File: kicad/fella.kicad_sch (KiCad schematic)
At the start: 0 parts

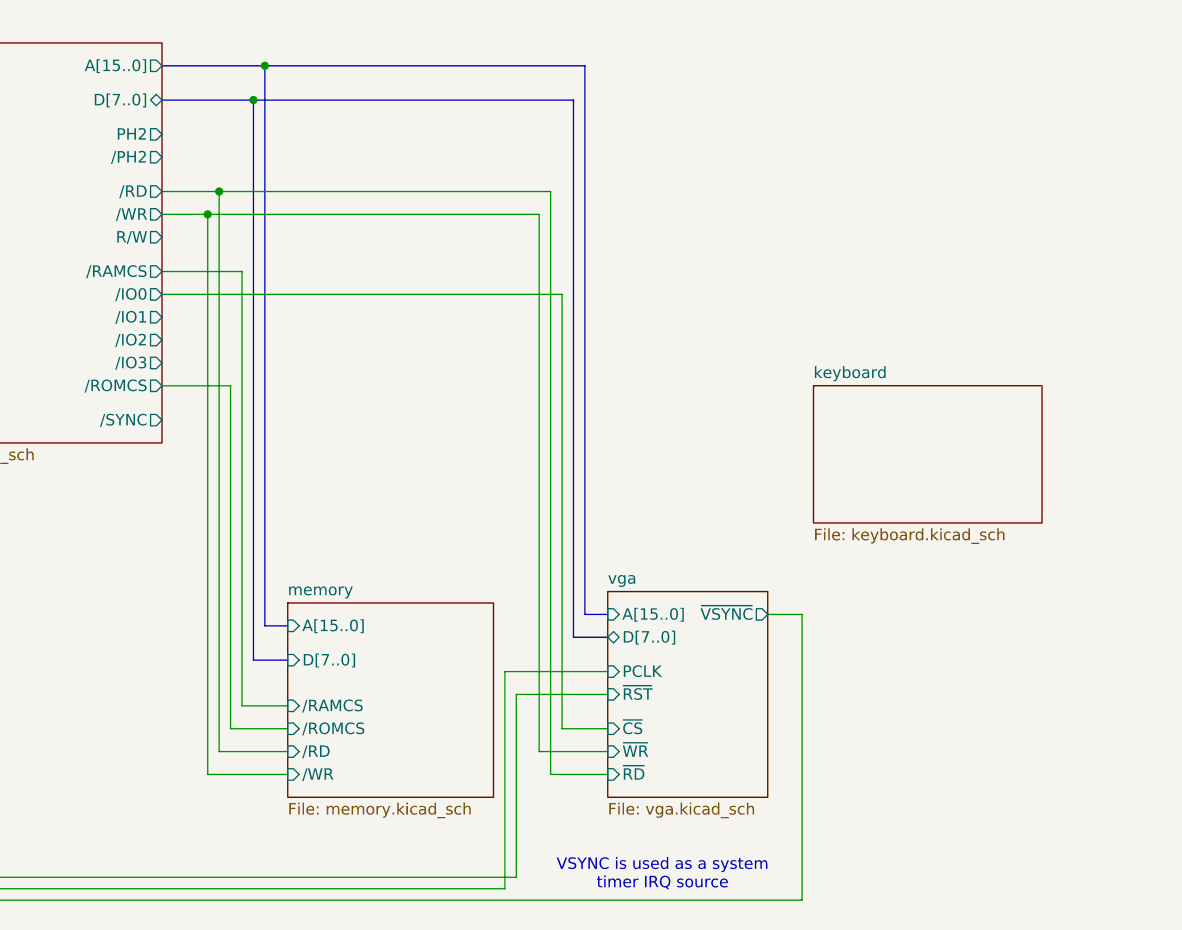
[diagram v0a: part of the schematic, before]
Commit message: Add keyboard connector
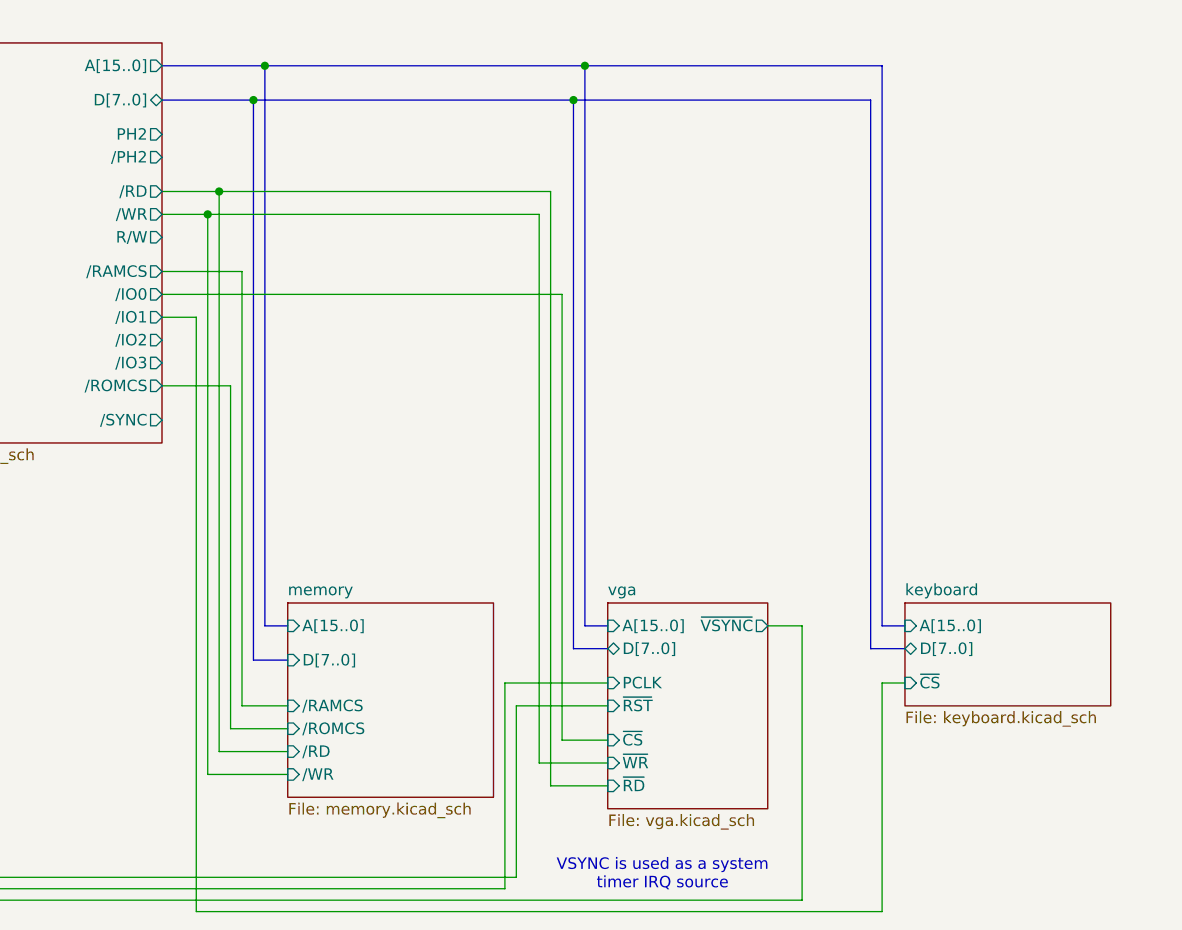
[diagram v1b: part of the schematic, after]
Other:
- sheet keyboard ports: added A[15..0], D[7..0], ~{CS}; removed none
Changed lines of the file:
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@@
+	)
+	(junction
+		(at 161.29 50.8)
+		(diameter 0)
+		(color 0 0 0 0)
 	)
 	(junction
@@
 		(color 0 0 0 0)
 	)
+	(junction
+		(at 160.02 54.61)
+		(diameter 0)
+		(color 0 0 0 0)
+	)
 	(wire
 		(pts
@@
 	(wire
 		(pts
-			(xy 181.61 111.76) (xy 185.42 111.76)
+			(xy 181.61 113.03) (xy 185.42 113.03)
 		)
 		(stroke
@@
 	(bus
 		(pts
-			(xy 161.29 111.76) (xy 161.29 50.8)
+			(xy 161.29 113.03) (xy 161.29 50.8)
 		)
 		(stroke
@@
 		)
 	)
+	(wire
+		(pts
+			(xy 114.3 78.74) (xy 118.11 78.74)
+		)
+		(stroke
+			(width 0)
+			(type default)
+		)
+	)
 	(bus
 		(pts
@@
 	(wire
 		(pts
-			(xy 156.21 67.31) (xy 156.21 127)
-		)
-		(stroke
-			(width 0)
-			(type default)
-		)
-	)
-	(bus
-		(pts
-			(xy 160.02 54.61) (xy 160.02 114.3)
+			(xy 156.21 67.31) (xy 156.21 128.27)
+		)
+		(stroke
+			(width 0)
+			(type default)
+		)
+	)
+	(bus
+		(pts
+			(xy 160.02 54.61) (xy 160.02 115.57)
 		)
 		(stroke
@@
 		)
 	)
+	(bus
+		(pts
+			(xy 194.31 50.8) (xy 161.29 50.8)
+		)
+		(stroke
+			(width 0)
+			(type default)
+		)
+	)
+	(bus
+		(pts
+			(xy 160.02 54.61) (xy 193.04 54.61)
+		)
+		(stroke
+			(width 0)
+			(type default)
+		)
+	)
 	(wire
 		(pts
@@
 	(bus
 		(pts
-			(xy 160.02 114.3) (xy 163.83 114.3)
-		)
-		(stroke
-			(width 0)
-			(type default)
-		)
-	)
-	(wire
-		(pts
-			(xy 158.75 124.46) (xy 163.83 124.46)
+			(xy 193.04 115.57) (xy 196.85 115.57)
+		)
+		(stroke
+			(width 0)
+			(type default)
+		)
+	)
+	(bus
+		(pts
+			(xy 160.02 115.57) (xy 163.83 115.57)
+		)
+		(stroke
+			(width 0)
+			(type default)
+		)
+	)
+	(wire
+		(pts
+			(xy 158.75 125.73) (xy 163.83 125.73)
+		)
+		(stroke
+			(width 0)
+			(type default)
+		)
+	)
+	(bus
+		(pts
+			(xy 193.04 54.61) (xy 193.04 115.57)
+		)
+		(stroke
+			(width 0)
+			(type default)
+		)
+	)
+	(wire
+		(pts
+			(xy 194.31 144.78) (xy 194.31 119.38)
 		)
 		(stroke
@@
 	(wire
 		(pts
-			(xy 157.48 129.54) (xy 163.83 129.54)
+			(xy 157.48 130.81) (xy 163.83 130.81)
+		)
+		(stroke
+			(width 0)
+			(type default)
+		)
+	)
+	(wire
+		(pts
+			(xy 118.11 78.74) (xy 118.11 144.78)
 		)
 		(stroke
@@
 	(wire
 		(pts
+			(xy 194.31 119.38) (xy 196.85 119.38)
+		)
+		(stroke
+			(width 0)
+			(type default)
+		)
+	)
+	(wire
+		(pts
 			(xy 119.38 67.31) (xy 119.38 129.54)
 		)
@@
 		)
 	)
+	(bus
+		(pts
+			(xy 196.85 113.03) (xy 194.31 113.03)
+		)
+		(stroke
+			(width 0)
+			(type default)
+		)
+	)
 	(wire
 		(pts
@@
 	(wire
 		(pts
-			(xy 158.75 76.2) (xy 158.75 124.46)
+			(xy 118.11 144.78) (xy 194.31 144.78)
+		)
+		(stroke
+			(width 0)
+			(type default)
+		)
+	)
+	(wire
+		(pts
+			(xy 158.75 76.2) (xy 158.75 125.73)
 		)
 		(stroke
@@
 	(wire
 		(pts
-			(xy 153.67 140.97) (xy 153.67 120.65)
+			(xy 153.67 140.97) (xy 153.67 121.92)
 		)
 		(stroke
@@
 	(wire
 		(pts
-			(xy 156.21 127) (xy 163.83 127)
-		)
-		(stroke
-			(width 0)
-			(type default)
-		)
-	)
-	(wire
-		(pts
-			(xy 153.67 120.65) (xy 163.83 120.65)
-		)
-		(stroke
-			(width 0)
-			(type default)
-		)
-	)
-	(wire
-		(pts
-			(xy 152.4 118.11) (xy 163.83 118.11)
-		)
-		(stroke
-			(width 0)
-			(type default)
-		)
-	)
-	(bus
-		(pts
-			(xy 163.83 111.76) (xy 161.29 111.76)
-		)
-		(stroke
-			(width 0)
-			(type default)
-		)
-	)
-	(wire
-		(pts
-			(xy 185.42 111.76) (xy 185.42 143.51)
+			(xy 156.21 128.27) (xy 163.83 128.27)
+		)
+		(stroke
+			(width 0)
+			(type default)
+		)
+	)
+	(wire
+		(pts
+			(xy 153.67 121.92) (xy 163.83 121.92)
+		)
+		(stroke
+			(width 0)
+			(type default)
+		)
+	)
+	(wire
+		(pts
+			(xy 152.4 119.38) (xy 163.83 119.38)
+		)
+		(stroke
+			(width 0)
+			(type default)
+		)
+	)
+	(bus
+		(pts
+			(xy 163.83 113.03) (xy 161.29 113.03)
+		)
+		(stroke
+			(width 0)
+			(type default)
+		)
+	)
+	(wire
+		(pts
+			(xy 185.42 113.03) (xy 185.42 143.51)
 		)
 		(stroke
@@
 	(bus
 		(pts
+			(xy 194.31 113.03) (xy 194.31 50.8)
+		)
+		(stroke
+			(width 0)
+			(type default)
+		)
+	)
+	(bus
+		(pts
 			(xy 114.3 50.8) (xy 125.73 50.8)
 		)
@@
 	(wire
 		(pts
-			(xy 152.4 142.24) (xy 152.4 118.11)
-		)
-		(stroke
-			(width 0)
-			(type default)
-		)
-	)
-	(wire
-		(pts
-			(xy 157.48 64.77) (xy 157.48 129.54)
+			(xy 152.4 142.24) (xy 152.4 119.38)
+		)
+		(stroke
+			(width 0)
+			(type default)
+		)
+	)
+	(wire
+		(pts
+			(xy 157.48 64.77) (xy 157.48 130.81)
 		)
 		(stroke
@@
 	)
 	(sheet
-		(at 186.69 86.36)
-		(size 25.4 15.24)
+		(at 196.85 110.49)
+		(size 22.86 11.43)
 		(fields_autoplaced yes)
 		(stroke
@@
 		)
 		(property "Sheetname" "keyboard"
-			(at 186.69 85.6484 0)
+			(at 196.85 109.7784 0)
 			(effects
 				(font
@@
 		)
 		(property "Sheetfile" "keyboard.kicad_sch"
-			(at 186.69 102.1846 0)
+			(at 196.85 122.5046 0)
 			(effects
 				(font
@@
 				)
 				(justify left top)
+			)
+		)
+		(pin "A[15..0]" input
+			(at 196.85 113.03 180)
+			(effects
+				(font
+					(size 1.27 1.27)
+				)
+				(justify left)
+			)
+		)
+		(pin "~{CS}" input
+			(at 196.85 119.38 180)
+			(effects
+				(font
+					(size 1.27 1.27)
+				)
+				(justify left)
+			)
+		)
+		(pin "D[7..0]" tri_state
+			(at 196.85 115.57 180)
+			(effects
+				(font
+					(size 1.27 1.27)
+				)
+				(justify left)
 			)
 		)
@@
 	)
 	(sheet
-		(at 163.83 109.22)
+		(at 163.83 110.49)
 		(size 17.78 22.86)
 		(fields_autoplaced yes)
@@
 		)
 		(property "Sheetname" "vga"
-			(at 163.83 108.5084 0)
+			(at 163.83 109.7784 0)
 			(effects
 				(font
@@
 		)
 		(property "Sheetfile" "vga.kicad_sch"
-			(at 163.83 132.6646 0)
+			(at 163.83 133.9346 0)
 			(effects
 				(font
@@
 		)
 		(pin "~{RST}" input
-			(at 163.83 120.65 180)
+			(at 163.83 121.92 180)
 			(effects
 				(font
@@
 		)
 		(pin "PCLK" input
-			(at 163.83 118.11 180)
+			(at 163.83 119.38 180)
 			(effects
 				(font
@@
 		)
 		(pin "~{WR}" input
-			(at 163.83 127 180)
+			(at 163.83 128.27 180)
 			(effects
 				(font
@@
 		)
 		(pin "A[15..0]" input
-			(at 163.83 111.76 180)
+			(at 163.83 113.03 180)
 			(effects
 				(font
@@
 		)
 		(pin "D[7..0]" bidirectional
-			(at 163.83 114.3 180)
+			(at 163.83 115.57 180)
 			(effects
 				(font
@@
 		)
 		(pin "~{RD}" input
-			(at 163.83 129.54 180)
+			(at 163.83 130.81 180)
 			(effects
 				(font
@@
 		)
 		(pin "~{CS}" input
-			(at 163.83 124.46 180)
+			(at 163.83 125.73 180)
 			(effects
 				(font
@@
 		)
 		(pin "~{VSYNC}" output
-			(at 181.61 111.76 0)
-			(effects
-				(font
+			(at 181.61 113.03 0)
+			(effects
+				(font

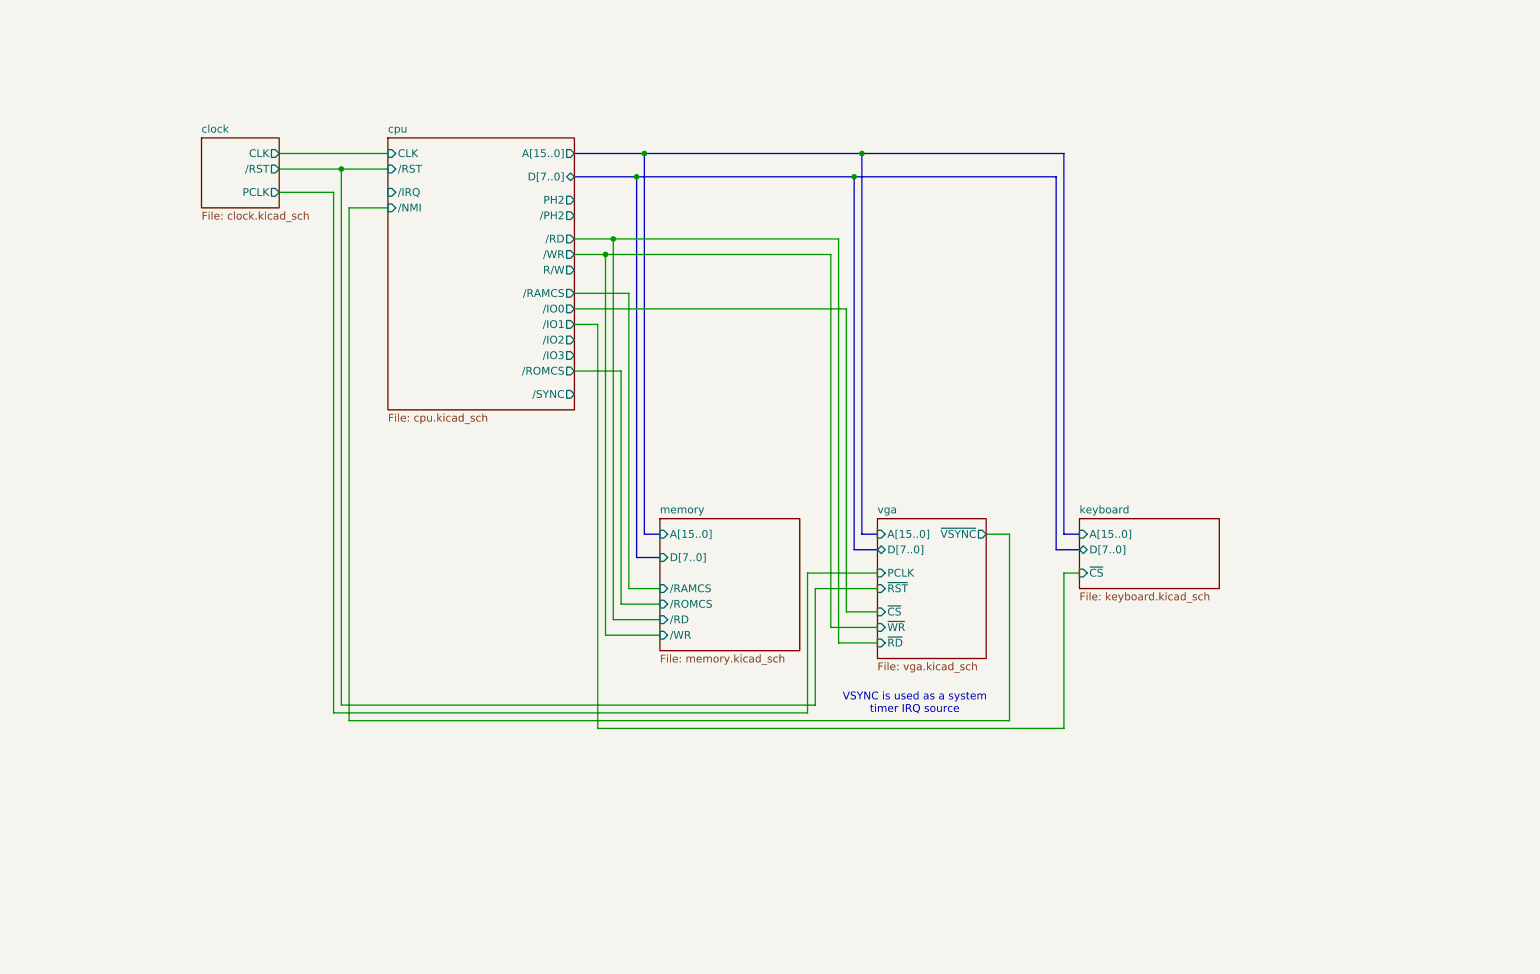
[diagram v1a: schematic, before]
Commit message: Add user IO and USB
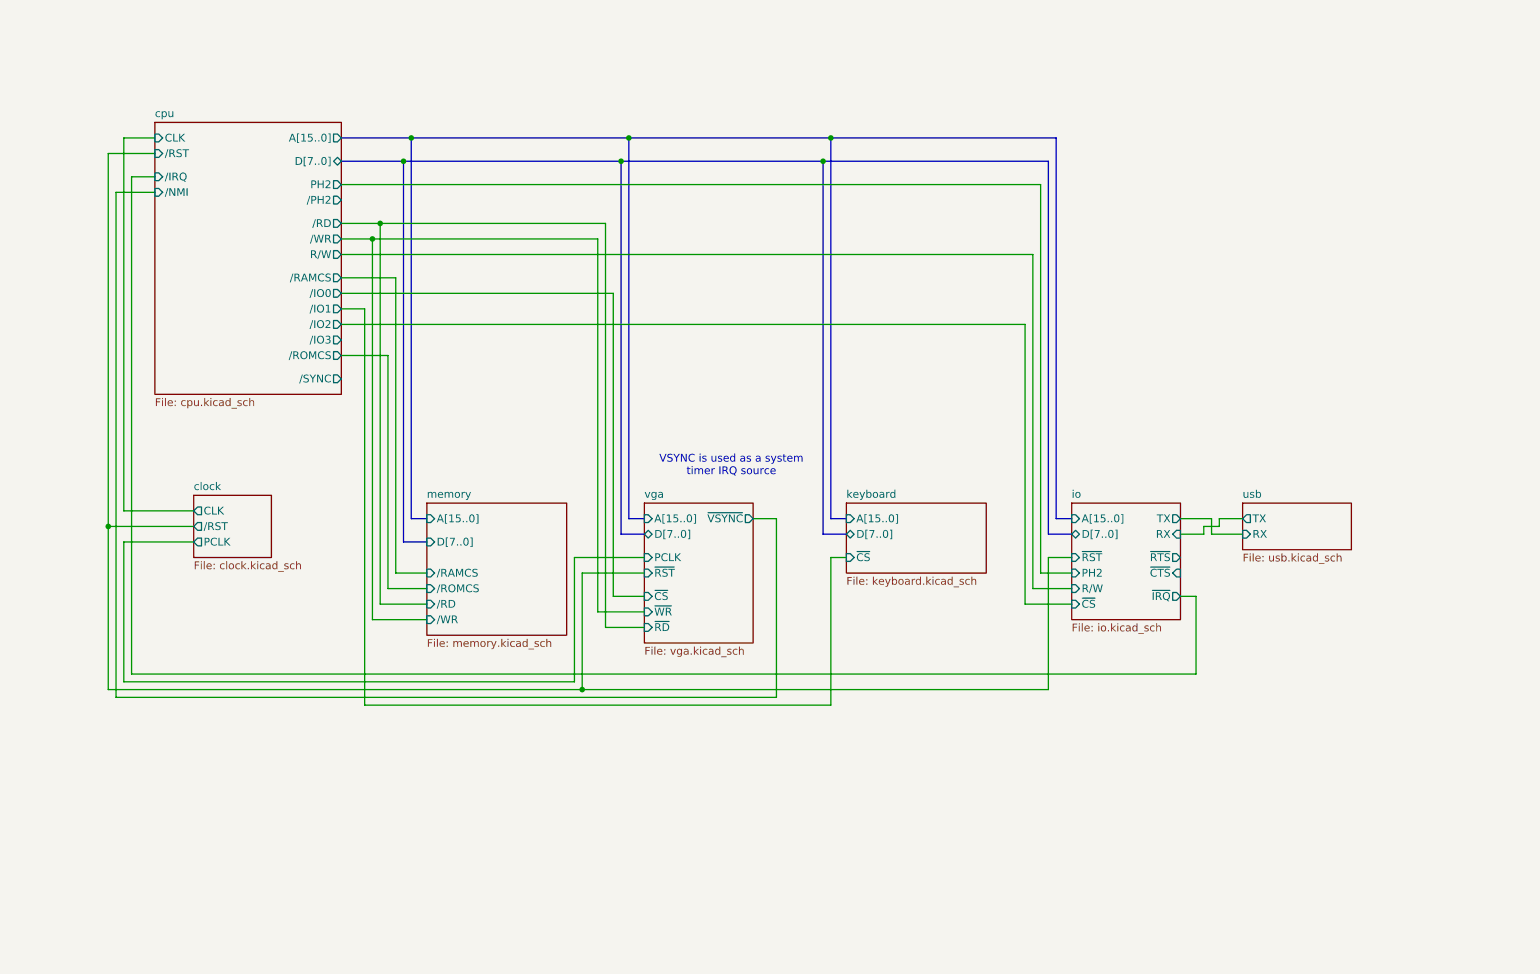
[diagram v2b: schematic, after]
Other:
- added sheet io (io.kicad_sch)
- added sheet usb (usb.kicad_sch)

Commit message: Add expansion slot
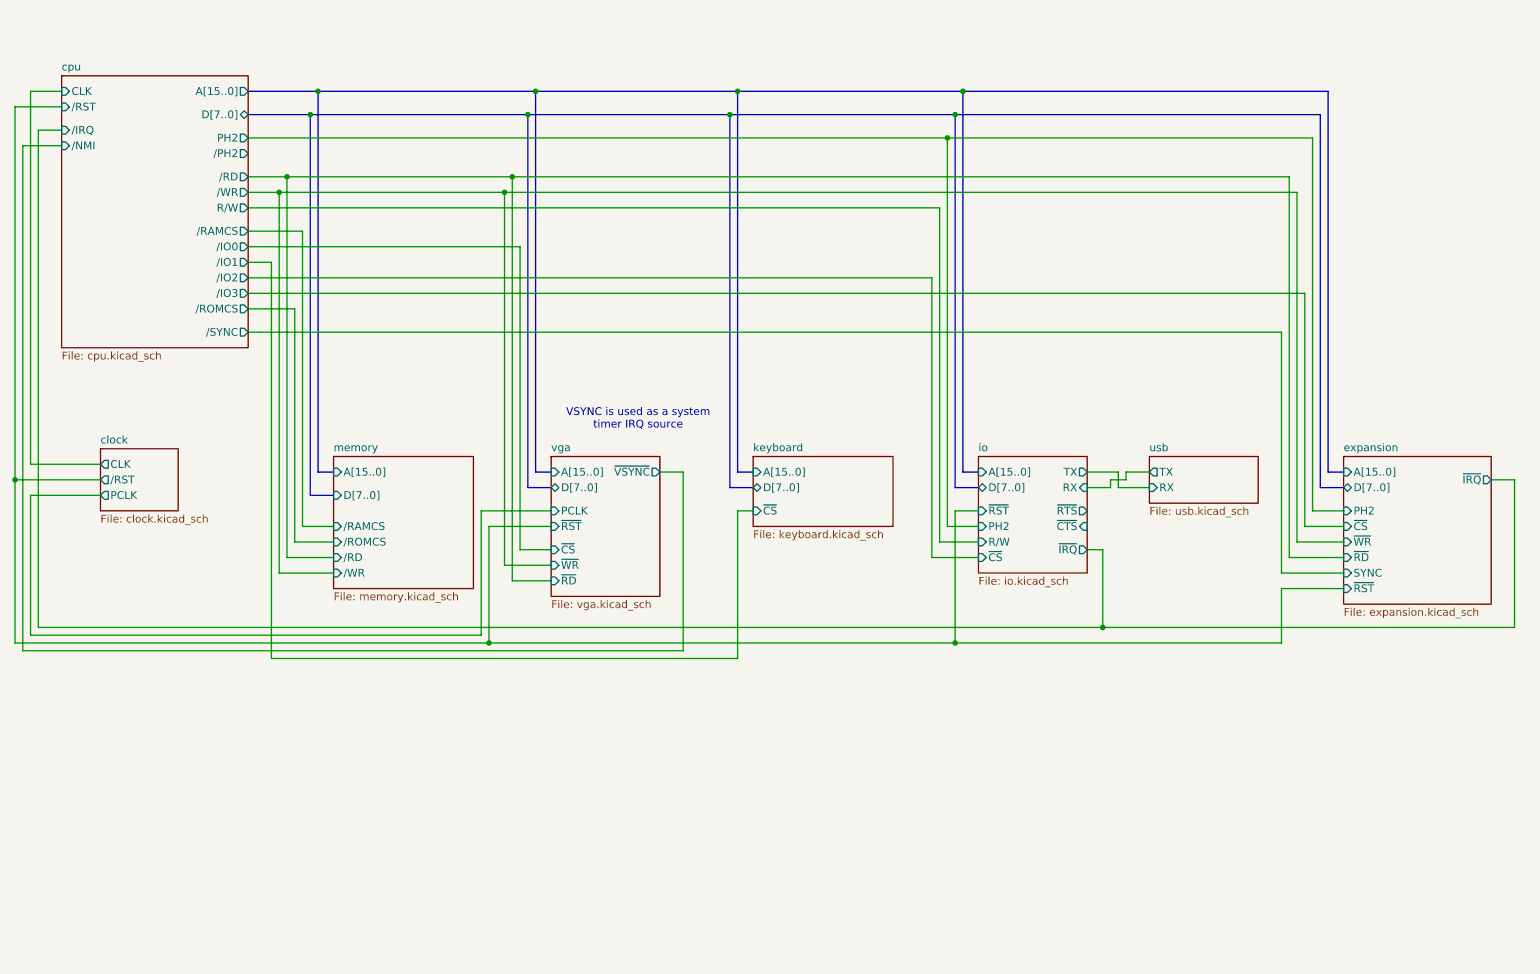
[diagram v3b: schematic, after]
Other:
- added sheet expansion (expansion.kicad_sch)

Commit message: Bugfixes, start routing
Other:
- sheet io ports: added ROMSEL0, ROMSEL1; removed none
- sheet vga ports: added ROMSEL0, ROMSEL1; removed none
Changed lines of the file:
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@@
+	(wire
+		(pts
+			(xy 128.27 121.92) (xy 180.34 121.92)
+		)
+		(stroke
+			(width 0)
+			(type default)
+		)
+	)
 	(wire
 		(pts
@@
 		(pts
 			(xy 106.68 44.45) (xy 106.68 105.41)
+		)
+		(stroke
+			(width 0)
+			(type default)
+		)
+	)
+	(wire
+		(pts
+			(xy 128.27 119.38) (xy 180.34 119.38)
 		)
 		(stroke
@@
 	(sheet
 		(at 180.34 100.33)
-		(size 17.78 19.05)
+		(size 17.78 24.13)
 		(fields_autoplaced yes)
 		(stroke
@@
 		)
 		(property "Sheetfile" "io.kicad_sch"
-			(at 180.34 119.9646 0)
+			(at 180.34 125.0446 0)
 			(effects
 				(font
@@
 				)
 				(justify right)
+			)
+		)
+		(pin "ROMSEL0" output
+			(at 180.34 119.38 180)
+			(effects
+				(font
+					(size 1.27 1.27)
+				)
+				(justify left)
+			)
+		)
+		(pin "ROMSEL1" output
+			(at 180.34 121.92 180)
+			(effects
+				(font
+					(size 1.27 1.27)
+				)
+				(justify left)
 			)
 		)
@@
 	(sheet
 		(at 110.49 100.33)
-		(size 17.78 22.86)
+		(size 17.78 24.13)
 		(fields_autoplaced yes)
 		(stroke
@@
 		)
 		(property "Sheetfile" "vga.kicad_sch"
-			(at 110.49 123.7746 0)
+			(at 110.49 125.0446 0)
 			(effects
 				(font
@@
 			(effects
 				(font
+					(size 1.27 1.27)
+				)
+				(justify right)
+			)
+		)
+		(pin "ROMSEL1" input
+			(at 128.27 121.92 0)
+			(effects
+				(font
+					(size 1.27 1.27)
+				)
+				(justify right)
+			)
+		)
+		(pin "ROMSEL0" input
+			(at 128.27 119.38 0)
+			(effects
+				(font

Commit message: Board outline
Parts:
- added H1, H2, H3, H4: MountingHole_Pad, MountingHole:MountingHole_3.2mm_M3_Pad_Via, symbol Mechanical:MountingHole_Pad
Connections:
- new net GND: H1.1, H2.1, H3.1, H4.1
